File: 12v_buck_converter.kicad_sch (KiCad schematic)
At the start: 25 parts, among them IC1 TPS56A37RPAR, Q4 SI7149ADP-T1-GE3, Q5 SI7149ADP-T1-GE3, U3 MAX16914AUB/V+T

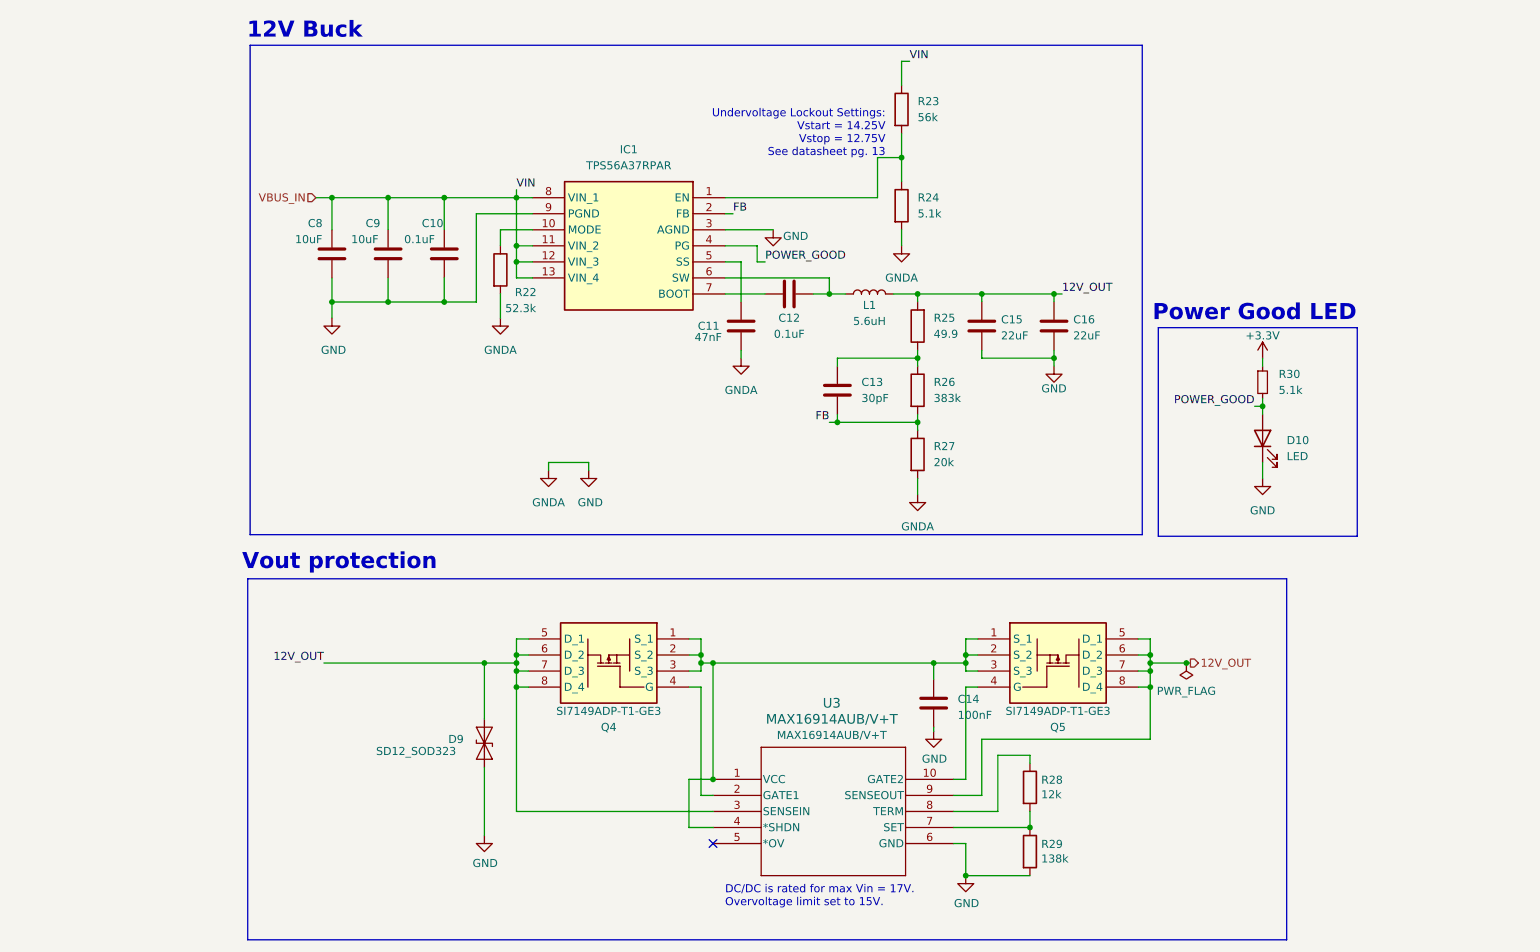
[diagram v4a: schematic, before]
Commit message: finished addressing review comments & organized bom with p/ns for everything
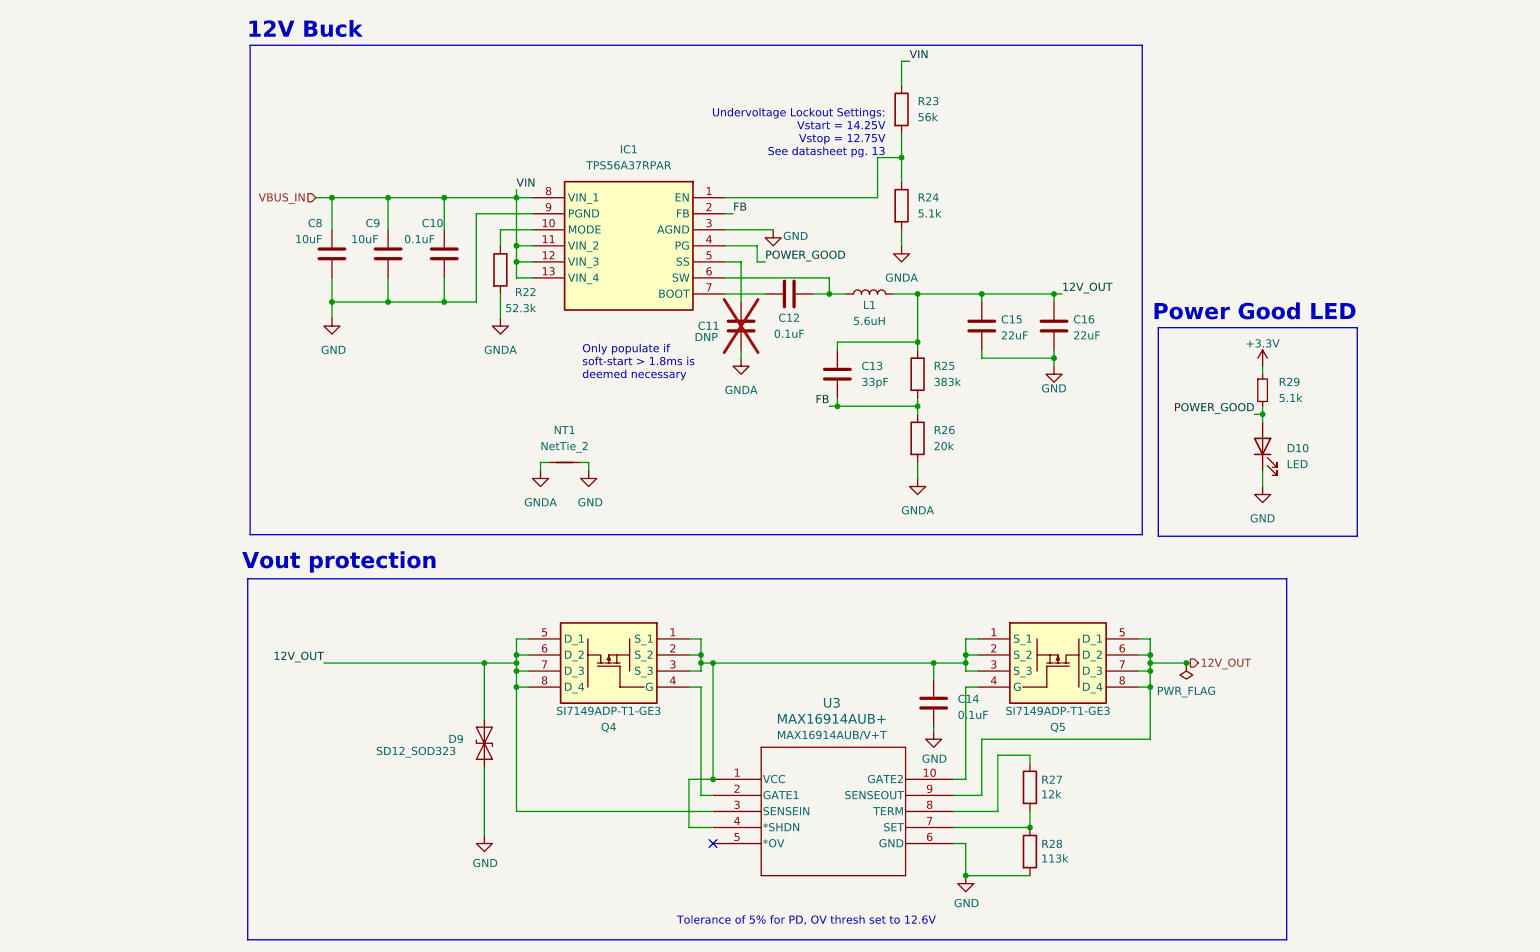
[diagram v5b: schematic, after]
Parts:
- removed R25: 49.9, Resistor_SMD:R_0805_2012Metric, symbol Device:R
- added NT1: NetTie_2, symbol Device:NetTie_2
- C10, C12: Manufacturer_Name (none) -> KEMET; Mouser Part Number (none) -> C0805C104M5RACTU; Vdc (none) -> 50V
- C11: value 47nF -> DNP; Manufacturer_Name (none) -> KEMET; now not fitted
- C13: value 30pF -> 33pF; Manufacturer_Name (none) -> KEMET; Mouser Part Number (none) -> C0805C330K5RACTU; Vdc (none) -> 50V
- C14: value 100nF -> 0.1uF; Manufacturer_Name (none) -> KEMET; Mouser Part Number 80-C0805C104M5R -> C0805C104M5RACTU; Vdc (none) -> 50V
- C15, C16: Manufacturer_Name (none) -> TDK; Mouser Part Number (none) -> C2012X5R1V226M125AC; Vdc (none) -> 35V
- C8, C9: Manufacturer_Name (none) -> KEMET; Mouser Part Number (none) -> C2220C106M5RACTU; Vdc (none) -> 50V
- D10: Manufacturer_Name (none) -> Kingbright; Mouser Part Number APTD2012LCGCK -> 604-APTD2012LCGCK
- D9: Manufacturer_Name (none) -> Semtech; Mouser Part Number (none) -> 947-SD12C.TCT
- L1: footprint UTSVT_Passive:INDPM135125X640N -> UTSVT_Passive:INDPM110100X400N; Manufacturer_Name (none) -> Bourns; Mouser Part Number SRP1265A-5R6M -> 652-SRP1038CC-5R6M
- Q4, Q5: Manufacturer_Name Vishay -> VISHAY
- R22: Manufacturer_Name (none) -> VISHAY; Mouser Part Number (none) -> CRCW080552K3FKEAC
- R23: Manufacturer_Name (none) -> VISHAY; Mouser Part Number (none) -> CRCW080556K0FKEAC
- R24: Manufacturer_Name (none) -> VISHAY; Mouser Part Number (none) -> CRCW08055K10FKEAC
- R25: renamed from R26; Manufacturer_Name (none) -> VISHAY; Mouser Part Number (none) -> CRCW0805383KFKEAC
- R26: renamed from R27; Manufacturer_Name (none) -> VISHAY; Mouser Part Number (none) -> CRCW080520K0FKEAC
- R27: renamed from R28; Manufacturer_Name (none) -> VISHAY; Mouser Part Number (none) -> CRCW080512K0FKEAC
- R28: renamed from R29; value 138k -> 113k; Manufacturer_Name (none) -> VISHAY; Mouser Part Number (none) -> CRCW0805113KFKEA
- R29: renamed from R30; Manufacturer_Name (none) -> VISHAY; Mouser Part Number (none) -> CRCW08055K10FKEAC
- U3: value MAX16914AUB/V+T -> MAX16914AUB+; Manufacturer_Name (none) -> Analog Devices; Mouser Part Number (none) -> 700-MAX16914AUB+
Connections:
- net 12V_OUT: now also C13.1, R25.1
- net GND: now also NT1.2; no longer C11.2, R22.2, R24.2, R26.2
- new net GNDA: C11.2, NT1.1, R22.2, R24.2, R26.2
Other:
- note added: "Only populate if soft-start > 1.8ms is deemed necessary"
- note added: "Tolerance of 5% for PD, OV thresh set to 12.6V"
- note removed: "DC/DC is rated for max Vin = 17V. Overvoltage limit set to 15V."
- title: (none) -> 12V Buck Converter
- moved on the sheet: C13, D10, R25, R26, R29

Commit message: intermediate progress push before addressing Champers' and Lakshay's review comments
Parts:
- C10: renamed from C9; footprint Capacitor_SMD:C_0805_2012Metric -> Capacitor_SMD:C_2220_5750Metric
- C9: renamed from C8; footprint Capacitor_SMD:C_0805_2012Metric -> Capacitor_SMD:C_2220_5750Metric
- NT1: footprint (none) -> NetTie:NetTie-2_SMD_Pad2.0mm
- renumbered C10 to C11, C11 to C12, C12 to C13, C13 to C14, C14 to C15, C15 to C16, C16 to C17
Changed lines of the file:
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@@
 		(dnp no)
 		(fields_autoplaced yes)
-		(property "Reference" "#PWR056"
+		(property "Reference" "#PWR055"
 			(at 144.78 77.47 0)
 			(effects
@@
 			(project ""
 				(path "/f58400c5-df4b-4929-8d2b-33c0fe23fcd9/01d27e83-9627-42d8-8cf9-628e44513f14"
-					(reference "#PWR056")
+					(reference "#PWR055")
 					(unit 1)
 				)
@@
 		(on_board yes)
 		(dnp no)
-		(property "Reference" "C15"
+		(property "Reference" "C16"
 			(at 185.928 65.024 0)
 			(effects
@@
 			(project "USBCPowerPCB"
 				(path "/f58400c5-df4b-4929-8d2b-33c0fe23fcd9/01d27e83-9627-42d8-8cf9-628e44513f14"
-					(reference "C15")
+					(reference "C16")
 					(unit 1)
 				)
@@
 		(on_board yes)
 		(dnp no)
-		(property "Reference" "#PWR055"
+		(property "Reference" "#PWR054"
 			(at 120.65 95.25 0)
 			(effects
@@
 			(project "USBCPowerPCB"
 				(path "/f58400c5-df4b-4929-8d2b-33c0fe23fcd9/01d27e83-9627-42d8-8cf9-628e44513f14"
-					(reference "#PWR055")
+					(reference "#PWR054")
 					(unit 1)
 				)
@@
 		(dnp no)
 		(fields_autoplaced yes)
-		(property "Reference" "#PWR058"
+		(property "Reference" "#PWR057"
 			(at 170.18 59.69 0)
 			(effects
@@
 			(project ""
 				(path "/f58400c5-df4b-4929-8d2b-33c0fe23fcd9/01d27e83-9627-42d8-8cf9-628e44513f14"
-					(reference "#PWR058")
+					(reference "#PWR057")
 					(unit 1)
 				)
@@
 		(dnp no)
 		(fields_autoplaced yes)
-		(property "Reference" "C13"
+		(property "Reference" "C14"
 			(at 163.83 72.3899 0)
 			(effects
@@
 			(project "USBCPowerPCB"
 				(path "/f58400c5-df4b-4929-8d2b-33c0fe23fcd9/01d27e83-9627-42d8-8cf9-628e44513f14"
-					(reference "C13")
+					(reference "C14")
 					(unit 1)
 				)
@@
 		(on_board yes)
 		(dnp yes)
-		(property "Reference" "C11"
+		(property "Reference" "C12"
 			(at 137.922 66.04 0)
 			(effects
@@
 			(project "USBCPowerPCB"
 				(path "/f58400c5-df4b-4929-8d2b-33c0fe23fcd9/01d27e83-9627-42d8-8cf9-628e44513f14"
-					(reference "C11")
+					(reference "C12")
 					(unit 1)
 				)
@@
 		(on_board yes)
 		(dnp no)
-		(property "Reference" "#PWR051"
+		(property "Reference" "#PWR050"
 			(at 80.01 71.12 0)
 			(effects
@@
 			(project "USBCPowerPCB"
 				(path "/f58400c5-df4b-4929-8d2b-33c0fe23fcd9/01d27e83-9627-42d8-8cf9-628e44513f14"
-					(reference "#PWR051")
+					(reference "#PWR050")
 					(unit 1)
 				)
@@
 		(dnp no)
 		(fields_autoplaced yes)
-		(property "Reference" "#PWR053"
+		(property "Reference" "#PWR052"
 			(at 106.68 71.12 0)
 			(effects
@@
 			(project ""
 				(path "/f58400c5-df4b-4929-8d2b-33c0fe23fcd9/01d27e83-9627-42d8-8cf9-628e44513f14"
-					(reference "#PWR053")
+					(reference "#PWR052")
 					(unit 1)
 				)
@@
 		(dnp no)
 		(fields_autoplaced yes)
-		(property "Reference" "#PWR064"
+		(property "Reference" "#PWR063"
 			(at 227.33 97.79 0)
 			(effects
@@
 			(project ""
 				(path "/f58400c5-df4b-4929-8d2b-33c0fe23fcd9/01d27e83-9627-42d8-8cf9-628e44513f14"
-					(reference "#PWR064")
+					(reference "#PWR063")
 					(unit 1)
 				)
@@
 		(on_board yes)
 		(dnp no)
-		(property "Reference" "#PWR060"
+		(property "Reference" "#PWR059"
 			(at 175.26 136.525 0)
 			(effects
@@
 			(project "USBCPowerPCB"
 				(path "/f58400c5-df4b-4929-8d2b-33c0fe23fcd9/01d27e83-9627-42d8-8cf9-628e44513f14"
-					(reference "#PWR060")
+					(reference "#PWR059")
 					(unit 1)
 				)
@@
 		(on_board yes)
 		(dnp no)
-		(property "Reference" "C12"
+		(property "Reference" "C13"
 			(at 152.4 64.77 90)
 			(effects
@@
 			(project "USBCPowerPCB"
 				(path "/f58400c5-df4b-4929-8d2b-33c0fe23fcd9/01d27e83-9627-42d8-8cf9-628e44513f14"
-					(reference "C12")
+					(reference "C13")
 					(unit 1)
 				)
@@
 		(on_board yes)
 		(dnp no)
-		(property "Reference" "#PWR062"
+		(property "Reference" "#PWR061"
 			(at 194.31 78.74 0)
 			(effects
@@
 			(project "USBCPowerPCB"
 				(path "/f58400c5-df4b-4929-8d2b-33c0fe23fcd9/01d27e83-9627-42d8-8cf9-628e44513f14"
-					(reference "#PWR062")
+					(reference "#PWR061")
 					(unit 1)
 				)
@@
 		(on_board yes)
 		(dnp no)
-		(property "Reference" "C16"
+		(property "Reference" "C17"
 			(at 197.358 65.024 0)
 			(effects
@@
 			(project "USBCPowerPCB"
 				(path "/f58400c5-df4b-4929-8d2b-33c0fe23fcd9/01d27e83-9627-42d8-8cf9-628e44513f14"
-					(reference "C16")
+					(reference "C17")
 					(unit 1)
 				)
@@
 		(on_board yes)
 		(dnp no)
-		(property "Reference" "#PWR063"
+		(property "Reference" "#PWR062"
 			(at 227.33 76.2 0)
 			(effects
@@
 			(project ""
 				(path "/f58400c5-df4b-4929-8d2b-33c0fe23fcd9/01d27e83-9627-42d8-8cf9-628e44513f14"
-					(reference "#PWR063")
+					(reference "#PWR062")
 					(unit 1)
 				)
@@
 		(dnp no)
 		(fields_autoplaced yes)
-		(property "Reference" "C14"
+		(property "Reference" "C15"
 			(at 179.07 125.095 0)
 			(effects
@@
 			(project "USBCPowerPCB"
 				(path "/f58400c5-df4b-4929-8d2b-33c0fe23fcd9/01d27e83-9627-42d8-8cf9-628e44513f14"
-					(reference "C14")
+					(reference "C15")
 					(unit 1)
 				)
@@
 		(dnp no)
 		(fields_autoplaced yes)
-		(property "Reference" "#PWR059"
+		(property "Reference" "#PWR058"
 			(at 172.72 96.52 0)
 			(effects
@@
 			(project "USBCPowerPCB"
 				(path "/f58400c5-df4b-4929-8d2b-33c0fe23fcd9/01d27e83-9627-42d8-8cf9-628e44513f14"
-					(reference "#PWR059")
+					(reference "#PWR058")
 					(unit 1)
 				)
@@
 		(on_board yes)
 		(dnp no)
-		(property "Reference" "C9"
+		(property "Reference" "C10"
 			(at 85.344 49.784 0)
 			(effects
@@
 			)
 		)
-		(property "Footprint" "Capacitor_SMD:C_0805_2012Metric"
+		(property "Footprint" "Capacitor_SMD:C_2220_5750Metric"
 			(at 89.8652 58.42 0)
 			(effects
@@
 			(project "USBCPowerPCB"
 				(path "/f58400c5-df4b-4929-8d2b-33c0fe23fcd9/01d27e83-9627-42d8-8cf9-628e44513f14"
-					(reference "C9")
+					(reference "C10")
 					(unit 1)
 				)
@@
 		(on_board yes)
 		(dnp no)
-		(property "Reference" "#PWR061"
+		(property "Reference" "#PWR060"
 			(at 180.34 159.385 0)
 			(effects
@@
 			(project "USBCPowerPCB"
 				(path "/f58400c5-df4b-4929-8d2b-33c0fe23fcd9/01d27e83-9627-42d8-8cf9-628e44513f14"
-					(reference "#PWR061")
+					(reference "#PWR060")
 					(unit 1)
 				)
@@
 		(on_board yes)
 		(dnp no)
-		(property "Reference" "C8"
+		(property "Reference" "C9"
 			(at 76.2 49.784 0)
 			(effects
@@
 			)
 		)
-		(property "Footprint" "Capacitor_SMD:C_0805_2012Metric"
+		(property "Footprint" "Capacitor_SMD:C_2220_5750Metric"
 			(at 80.9752 58.42 0)
 			(effects
@@
 			(project "USBCPowerPCB"
 				(path "/f58400c5-df4b-4929-8d2b-33c0fe23fcd9/01d27e83-9627-42d8-8cf9-628e44513f14"
-					(reference "C8")
+					(reference "C9")
 					(unit 1)
 				)
@@
 		(dnp no)
 		(fields_autoplaced yes)
-		(property "Reference" "#PWR054"
+		(property "Reference" "#PWR053"
 			(at 113.03 95.25 0)
 			(effects
@@
 			(project "USBCPowerPCB"
 				(path "/f58400c5-df4b-4929-8d2b-33c0fe23fcd9/01d27e83-9627-42d8-8cf9-628e44513f14"
-					(reference "#PWR054")
+					(reference "#PWR053")
 					(unit 1)
 				)
@@
 		(on_board yes)
 		(dnp no)
-		(property "Reference" "C10"
+		(property "Reference" "C11"
 			(at 94.234 49.784 0)
 			(effects
@@
 			(project "USBCPowerPCB"
 				(path "/f58400c5-df4b-4929-8d2b-33c0fe23fcd9/01d27e83-9627-42d8-8cf9-628e44513f14"
-					(reference "C10")
+					(reference "C11")
 					(unit 1)
 				)
@@
 			)
 		)
-		(property "Footprint" ""
+		(property "Footprint" "NetTie:NetTie-2_SMD_Pad2.0mm"
 			(at 116.84 87.63 0)
 			(effects
@@
 		(on_board yes)
 		(dnp no)
-		(property "Reference" "#PWR057"
+		(property "Reference" "#PWR056"
 			(at 149.86 57.15 0)
 			(effects
@@
 			(project "USBCPowerPCB"
 				(path "/f58400c5-df4b-4929-8d2b-33c0fe23fcd9/01d27e83-9627-42d8-8cf9-628e44513f14"
-					(reference "#PWR057")
+					(reference "#PWR056")
 					(unit 1)
 				)
@@
 		(on_board yes)
 		(dnp no)
-		(property "Reference" "#PWR052"
+		(property "Reference" "#PWR051"
 			(at 104.14 153.035 0)
 			(effects
@@
 			(project "USBCPowerPCB"
 				(path "/f58400c5-df4b-4929-8d2b-33c0fe23fcd9/01d27e83-9627-42d8-8cf9-628e44513f14"
-					(reference "#PWR052")
+					(reference "#PWR051")
 					(unit 1)
 				)
